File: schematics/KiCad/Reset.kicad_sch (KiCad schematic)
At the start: 8 parts, among them SW2 RESET, U13 74HC132, U9 74HC08

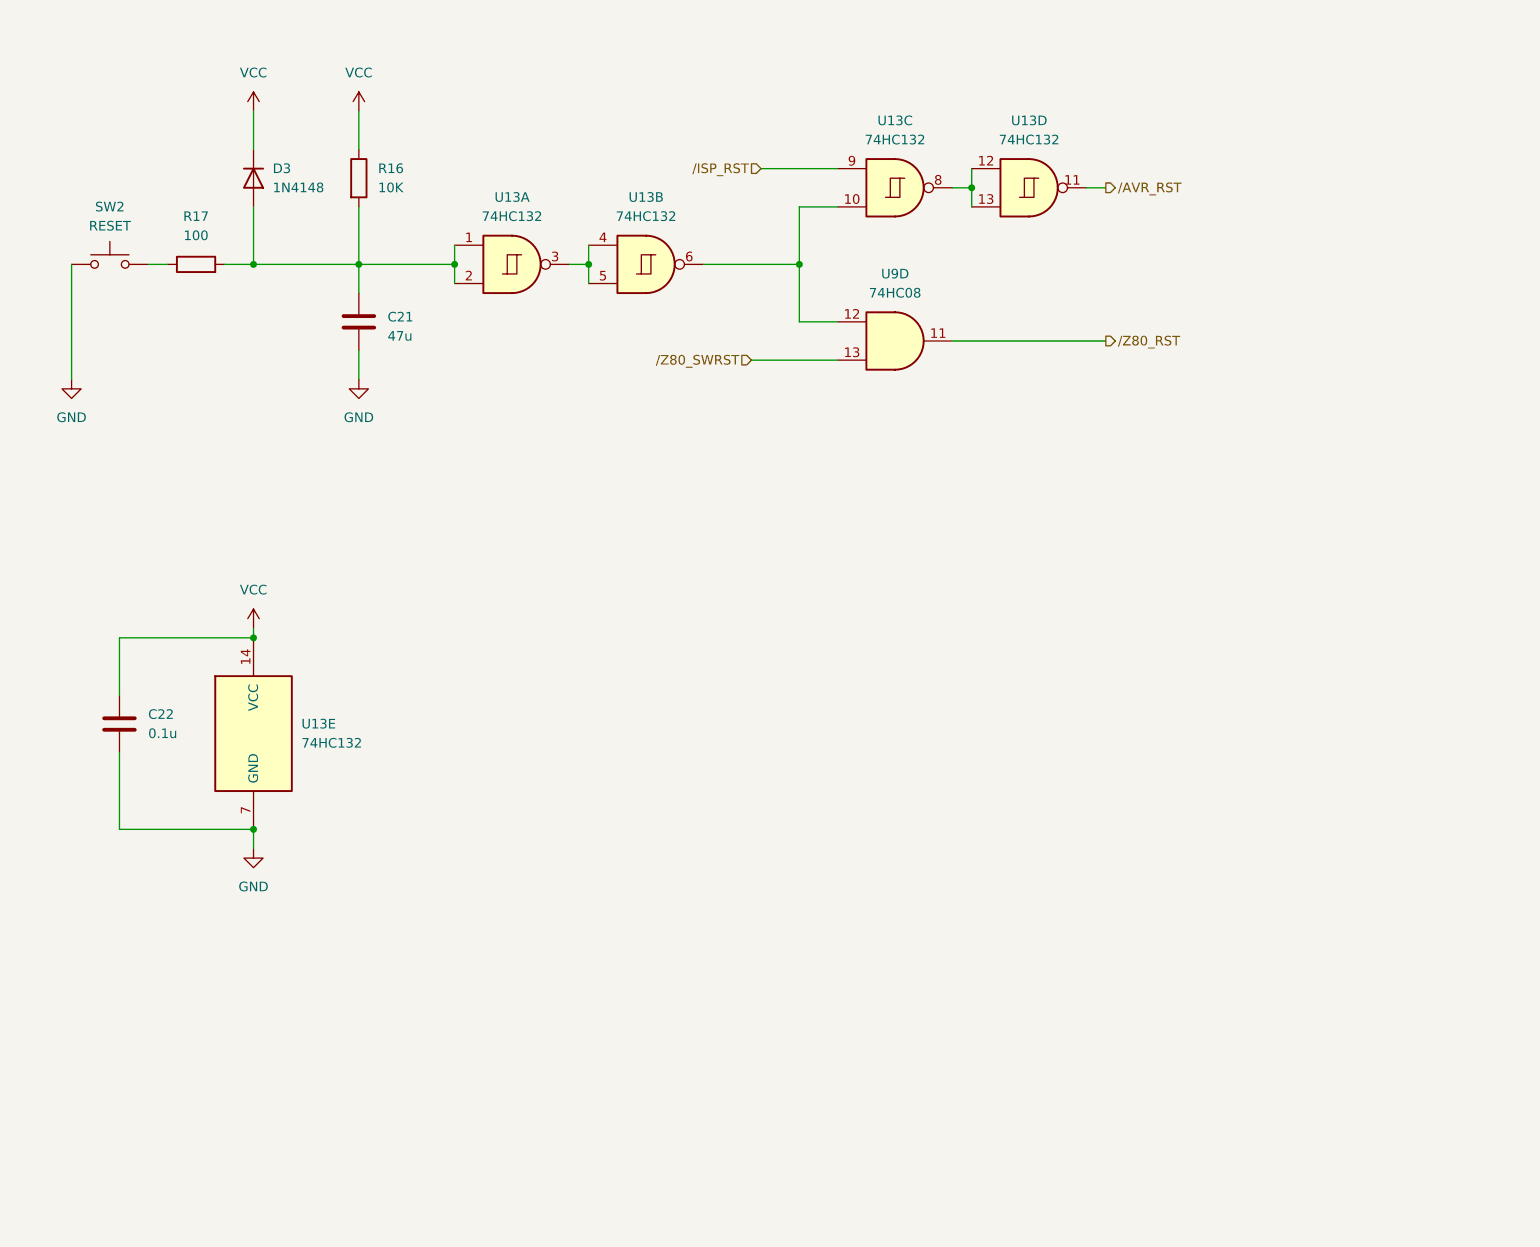
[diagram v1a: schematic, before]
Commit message: Update Reset circuit and Serial interface
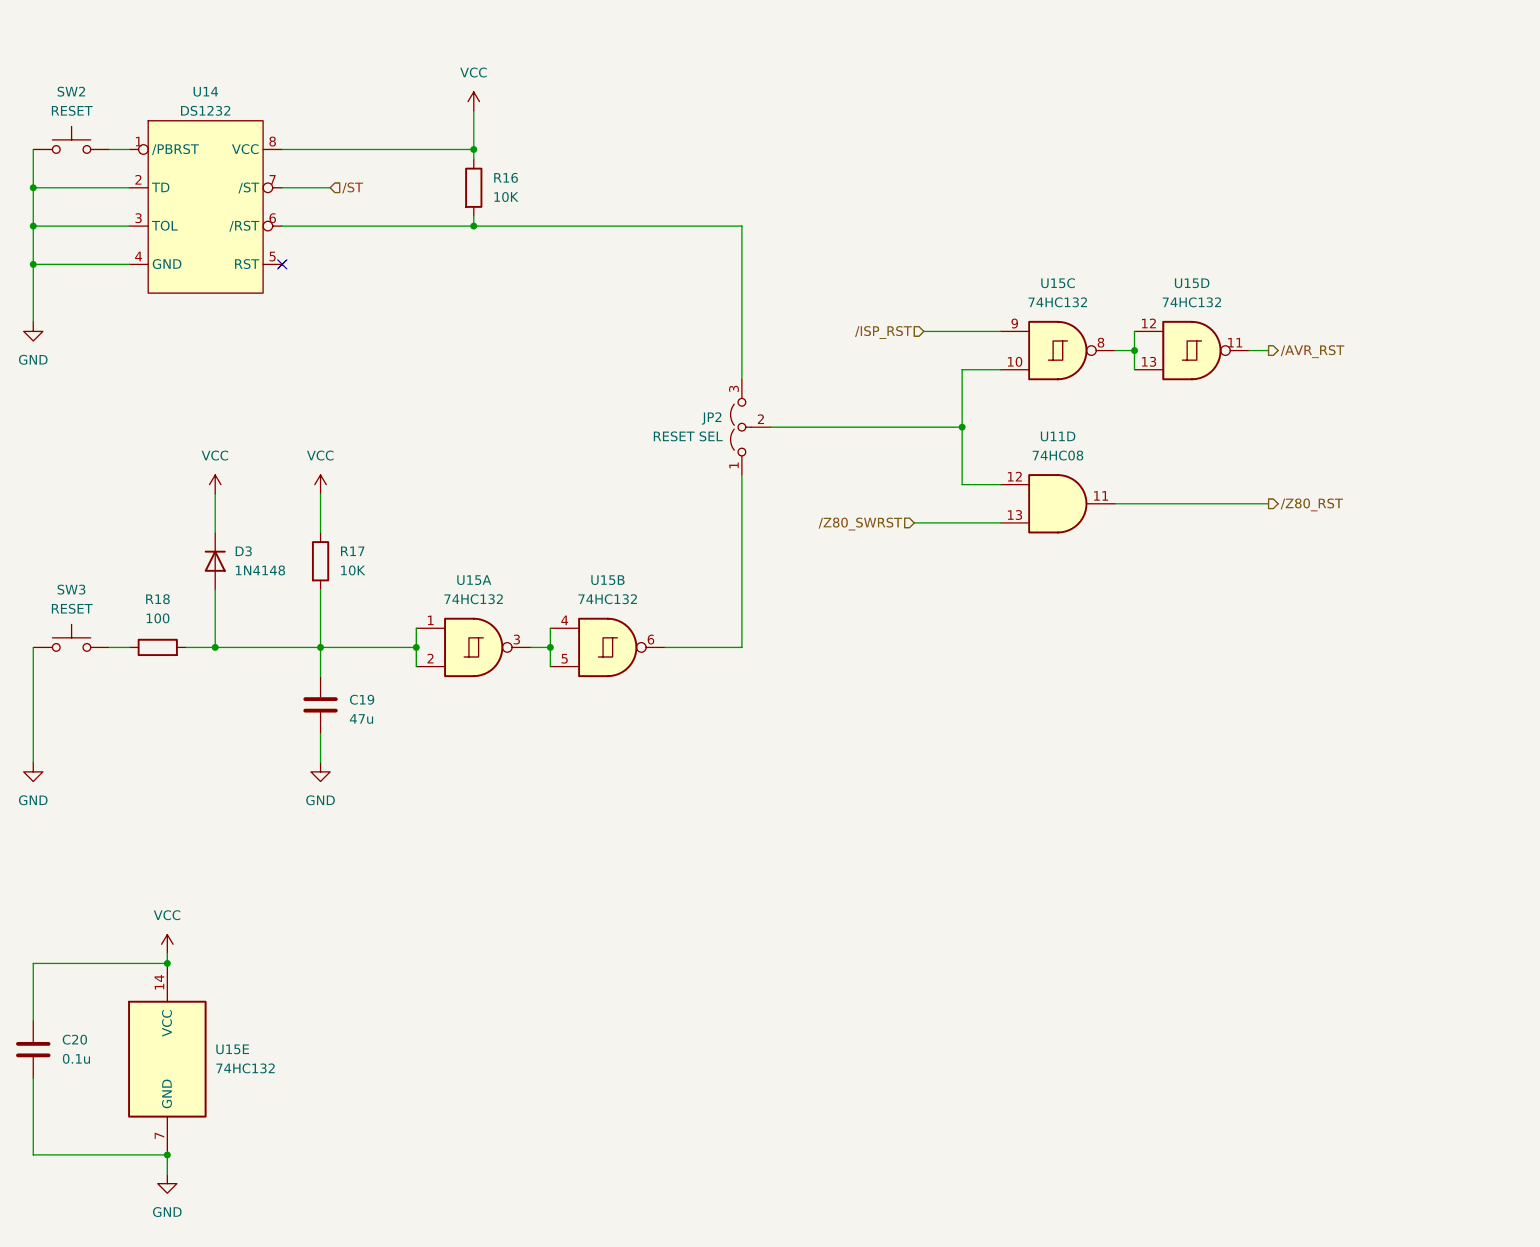
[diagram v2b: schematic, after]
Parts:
- added JP2: RESET SEL, Connector_PinHeader_2.54mm:PinHeader_1x03_P2.54mm_Vertical, symbol Jumper:Jumper_3_Open
- added R16: 10K, Resistor_THT:R_Axial_DIN0204_L3.6mm_D1.6mm_P7.62mm_Horizontal, symbol Device:R
- added SW2: RESET, Button_Switch_THT:SW_PUSH_6mm_H7.3mm, symbol Switch:SW_Push
- added U14: DS1232, Package_DIP:DIP-8_W7.62mm, symbol 46nori_Library:DS1232
- renumbered C21 to C19, C22 to C20, R16 to R17, R17 to R18, SW2 to SW3, U9 to U11, U13 to U15
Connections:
- net GND: now also SW2.1, U14.2 (TD), U14.3 (TOL), U14.4 (GND)
- net VCC: now also R16.1, U14.8 (VCC)
- net at U11.12, U15.10: now also JP2.2 (C); no longer U15.6
- new net: JP2.1 (A), U15.6
- new net: JP2.3 (B), R16.2, U14.6 (/RST)
- new net: SW2.2, U14.1 (/PBRST)
- new net /ST: U14.7 (/ST)
- no-connect marks 0 -> 1
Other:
- moved on the sheet: C19, C20, D3, R17, R18, SW3, U11D, U15A, U15B, U15C, U15D, U15E

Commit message: Update schematics.
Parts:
- added R18: 10K, Resistor_THT:R_Axial_DIN0204_L3.6mm_D1.6mm_P7.62mm_Horizontal, symbol Device:R
- renumbered R18 to R19
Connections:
- net GND: no longer U14.2 (TD)
- net VCC: now also U14.2 (TD), R18.2
- net /Z80_SWRST: now also R18.1
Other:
- company: (none) -> By 46nori
- moved on the sheet: C19, C20, D3, JP2, R16, R17, R19, SW2, SW3, U11D, U14, U15A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

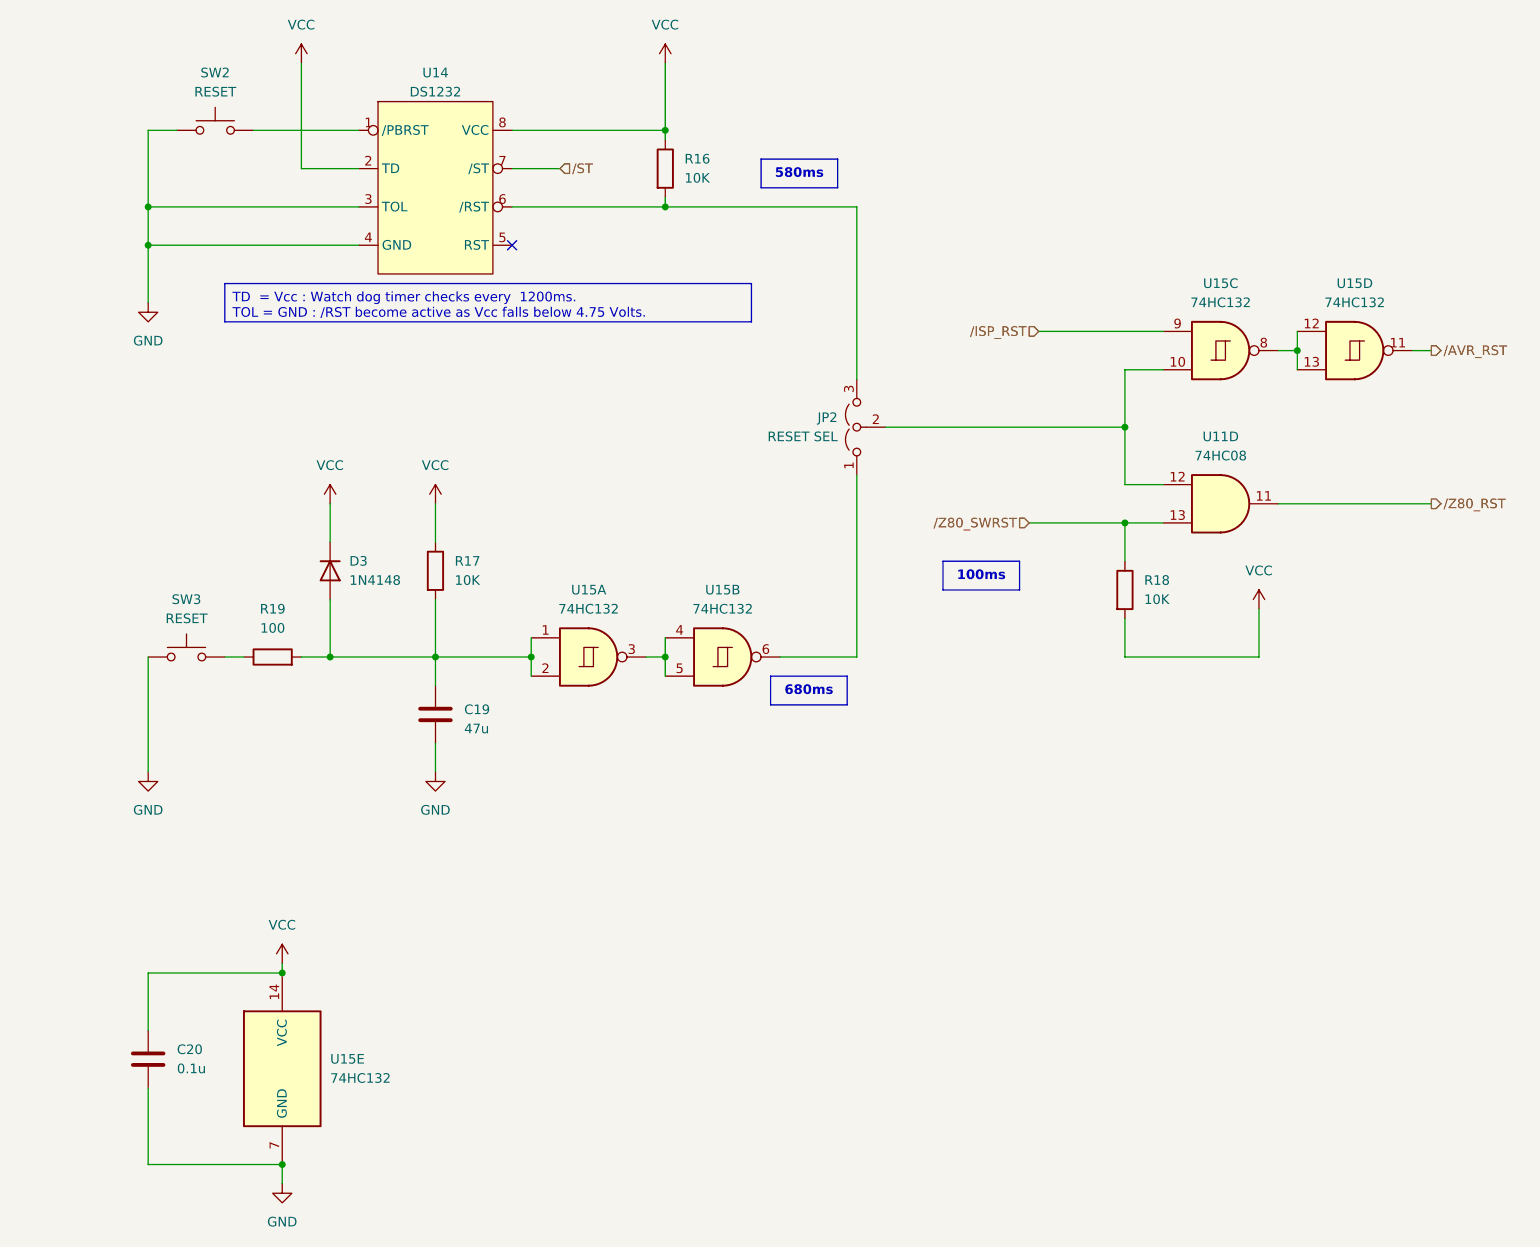
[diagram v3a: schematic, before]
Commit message: Update RESET circuit using DS1232N.
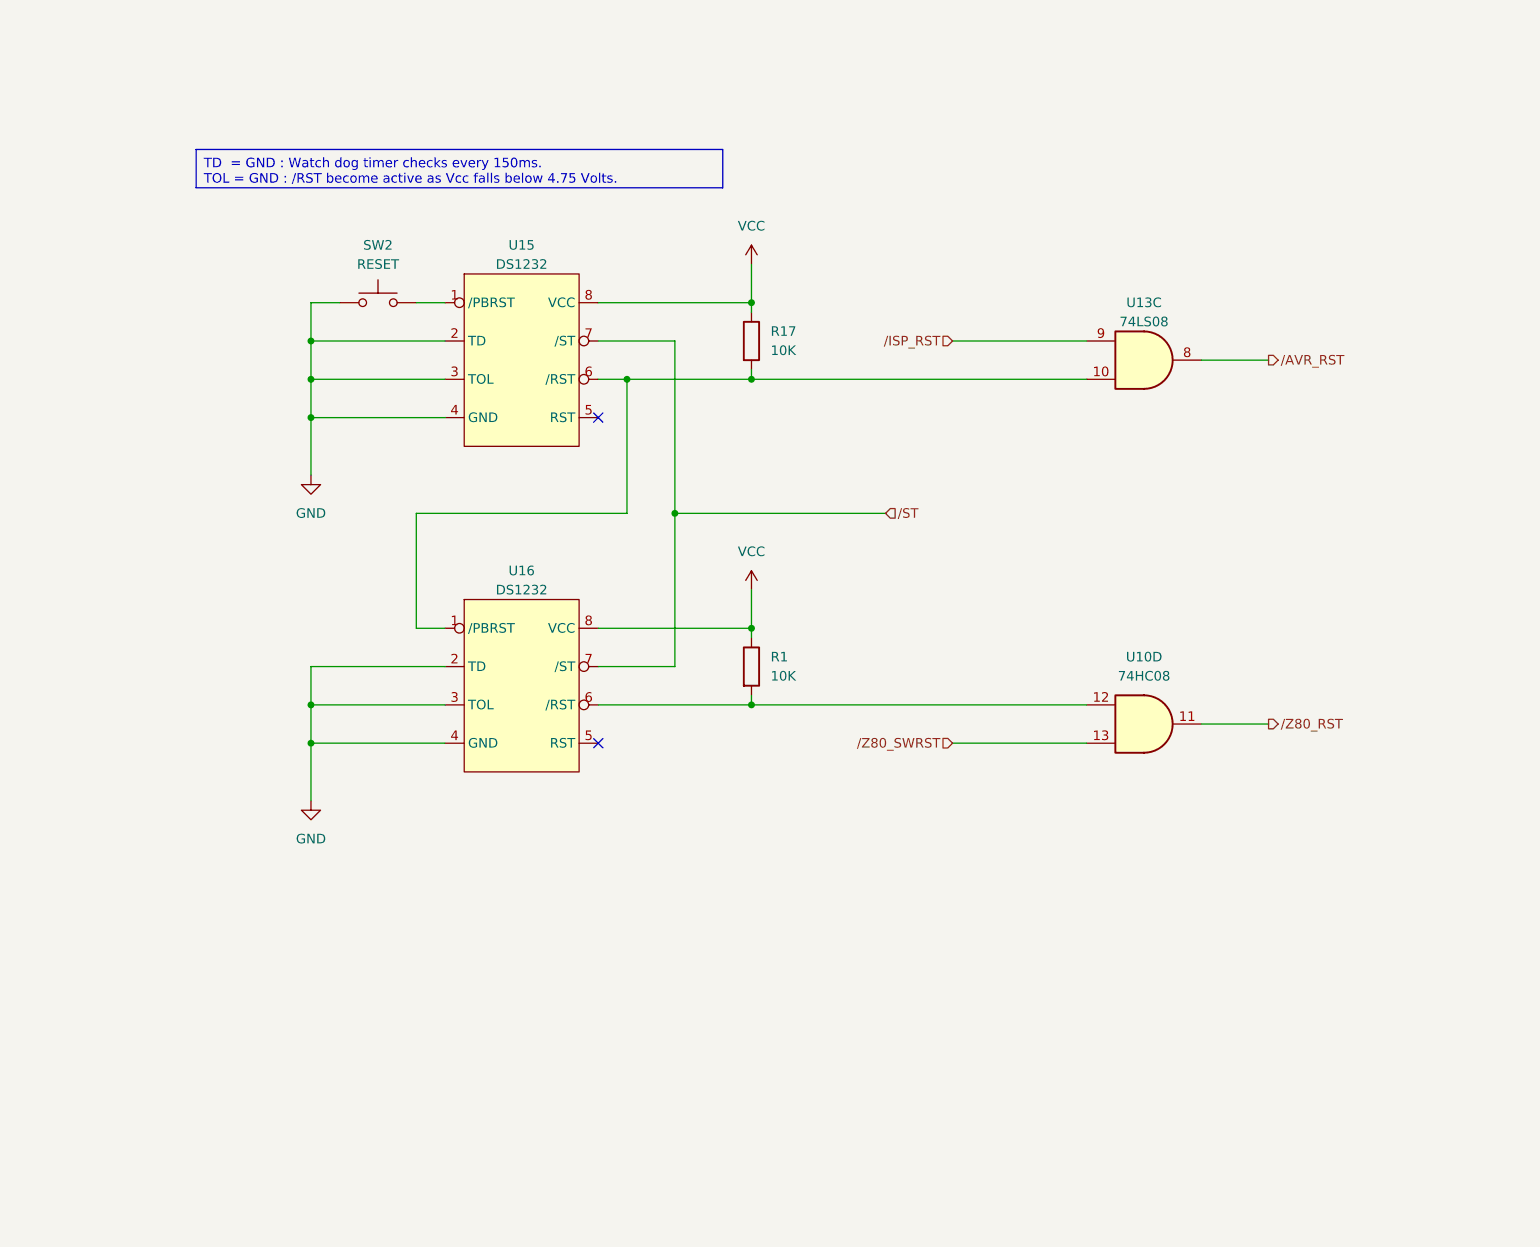
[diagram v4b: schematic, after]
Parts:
- removed C19: 47u, Capacitor_THT:CP_Radial_Tantal_D5.0mm_P2.50mm, symbol Device:C
- removed C20: 0.1u, Capacitor_THT:C_Disc_D3.8mm_W2.6mm_P2.50mm, symbol Device:C
- removed D3: 1N4148, Diode_THT:D_DO-35_SOD27_P7.62mm_Horizontal, symbol Diode:1N4148
- removed JP2: RESET SEL, Connector_PinHeader_2.54mm:PinHeader_1x03_P2.54mm_Vertical, symbol Jumper:Jumper_3_Open
- removed R17, R18: 10K, Resistor_THT:R_Axial_DIN0204_L3.6mm_D1.6mm_P7.62mm_Horizontal, symbol Device:R
- removed R19: 100, Resistor_THT:R_Axial_DIN0204_L3.6mm_D1.6mm_P7.62mm_Horizontal, symbol Device:R
- removed SW3: RESET, Button_Switch_THT:SW_PUSH_6mm_H7.3mm, symbol Switch:SW_Push
- removed U15: 74HC132, Package_DIP:DIP-14_W7.62mm_Socket, symbol 74xx:74LS132
- added R1: 10K, Resistor_THT:R_Axial_DIN0204_L3.6mm_D1.6mm_P7.62mm_Horizontal, symbol Device:R
- added U13: 74LS08, Package_DIP:DIP-14_W7.62mm_Socket, symbol 74xx:74LS08
- added U16: DS1232, Package_DIP:DIP-8_W7.62mm, symbol 46nori_Library:DS1232
- renumbered R16 to R17, U11 to U10, U14 to U15
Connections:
- net GND: now also U15.2 (TD), U16.2 (TD), U16.3 (TOL), U16.4 (GND)
- net VCC: now also R1.1, U16.8 (VCC); no longer U15.2 (TD)
- net /AVR_RST: now also U13.8
- net /ISP_RST: now also U13.9
- net /ST: now also U16.7 (/ST)
- net at U10.12: now also R1.2, U16.6 (/RST)
- net at R17.2, U15.6 (/RST): now also U13.10, U16.1 (/PBRST)
- no-connect marks 1 -> 2
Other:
- moved on the sheet: R17, SW2, U10D, U15
